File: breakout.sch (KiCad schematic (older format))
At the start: 8 parts, among them CON1 USB-MINI-B, P1 CONN_02X18, P2 CONN_02X18, P3 CONN_02X18, P4 CONN_02X18, P5 CONN_01X17, P6 CONN_01X02, U1 LPC4337JBD144

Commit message: adding components
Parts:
- removed P1, P2, P3, P4: CONN_02X18, Socket_Strips:Socket_Strip_Straight_2x18, symbol CONN_02X18
- removed P5: CONN_01X17, Housings_DFN_QFN:QFN-16-1EP_3x3mm_Pitch0.5mm, symbol CONN_01X17
- added U2: AP3003S-3.3TRE1, SMD_Packages:TO-263-5, symbol AP3003S-3.3TRE1
- added U3: A-DF-09-A/KG-T4S, Custom Footprints:DIN9F, symbol A-DF-09-A/KG-T4S
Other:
- note removed: "Microchip 3.3 V power regulator"
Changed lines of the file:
@@
 LIBS:valves
 LIBS:nxp
+LIBS:diodesinc
+LIBS:assmann
 LIBS:breakout-cache
 EELAYER 25 0
@@
 NoConn ~ 2800 850
 NoConn ~ 2800 950
-$Comp
-L USB-MINI-B CON1
-U 1 1 56013B96
-P 6200 5750
-F 0 "CON1" H 5900 6100 50  0000 C CNN
-F 1 "USB-MINI-B" H 6050 5400 50  0000 C CNN
-F 2 "Connect:USB_Mini-B" H 6200 5650 50  0001 C CNN
-F 3 "" H 6200 5650 50  0000 C CNN
-	1    6200 5750
-	1    0    0    1
-$EndComp
 Wire Wire Line
 	4800 5750 5450 5750
@@
 	5200 7450 4800 7450
 $Comp
-L CONN_02X18 P1
-U 1 1 55FF6B36
-P 1100 1700
-F 0 "P1" H 1100 2650 50  0000 C CNN
-F 1 "CONN_02X18" V 1100 1700 50  0000 C CNN
-F 2 "Socket_Strips:Socket_Strip_Straight_2x18" H 1100 650 60  0001 C CNN
-F 3 "" H 1100 650 60  0000 C CNN
-	1    1100 1700
-	1    0    0    -1
-$EndComp
-$Comp
-L CONN_02X18 P2
-U 1 1 55FF6C44
-P 1100 3650
-F 0 "P2" H 1100 4600 50  0000 C CNN
-F 1 "CONN_02X18" V 1100 3650 50  0000 C CNN
-F 2 "Socket_Strips:Socket_Strip_Straight_2x18" H 1100 2600 60  0001 C CNN
-F 3 "" H 1100 2600 60  0000 C CNN
-	1    1100 3650
-	1    0    0    -1
-$EndComp
-$Comp
-L CONN_02X18 P3
-U 1 1 55FF6CC4
-P 5750 1600
-F 0 "P3" H 5750 2550 50  0000 C CNN
-F 1 "CONN_02X18" V 5750 1600 50  0000 C CNN
-F 2 "Socket_Strips:Socket_Strip_Straight_2x18" H 5750 550 60  0001 C CNN
-F 3 "" H 5750 550 60  0000 C CNN
-	1    5750 1600
-	1    0    0    -1
-$EndComp
-$Comp
-L CONN_02X18 P4
-U 1 1 55FF6D42
-P 5750 3700
-F 0 "P4" H 5750 4650 50  0000 C CNN
-F 1 "CONN_02X18" V 5750 3700 50  0000 C CNN
-F 2 "Socket_Strips:Socket_Strip_Straight_2x18" H 5750 2650 60  0001 C CNN
-F 3 "" H 5750 2650 60  0000 C CNN
-	1    5750 3700
-	1    0    0    -1
-$EndComp
-$Comp
 L CONN_01X02 P6
 U 1 1 55FF7251
@@
 	-1   0    0    1
 $EndComp
-$Comp
-L CONN_01X17 P5
-U 1 1 55FF72F4
-P 7150 2850
-F 0 "P5" H 7150 3750 50  0000 C CNN
-F 1 "CONN_01X17" V 7250 2850 50  0000 C CNN
-F 2 "Housings_DFN_QFN:QFN-16-1EP_3x3mm_Pitch0.5mm" H 7150 2850 60  0001 C CNN
-F 3 "" H 7150 2850 60  0000 C CNN
-	1    7150 2850
-	-1   0    0    1
-$EndComp
 Text Notes 7450 750  0    60   ~ 0
 Power In
-Text Notes 6450 1950 0    60   ~ 0
-Microchip 3.3 V power regulator
+$Comp
+L USB-MINI-B CON1
+U 1 1 56013B96
+P 6200 5750
+F 0 "CON1" H 5900 6100 50  0000 C CNN
+F 1 "USB-MINI-B" H 6050 5400 50  0000 C CNN
+F 2 "Connect:USB_Mini-B" H 6200 5650 50  0001 C CNN
+F 3 "" H 6200 5650 50  0000 C CNN
+	1    6200 5750
+	1    0    0    1
+$EndComp
+$Comp
+L AP3003S-3.3TRE1 U2
+U 1 1 56145B14
+P 6750 2800
+F 0 "U2" H 6750 3750 60  0000 C CNN
+F 1 "AP3003S-3.3TRE1" H 6750 2800 60  0000 C CNN
+F 2 "SMD_Packages:TO-263-5" H 6750 2800 60  0001 C CNN
+F 3 "" H 6750 2800 60  0000 C CNN
+	1    6750 2800
+	1    0    0    -1
+$EndComp
+$Comp
+L A-DF-09-A/KG-T4S U3
+U 1 1 5614B4EE
+P 6400 3450
+F 0 "U3" H 6400 2750 60  0000 C CNN
+F 1 "A-DF-09-A/KG-T4S" H 6400 3450 60  0000 C CNN
+F 2 "Custom Footprints:DIN9F" H 6400 3450 60  0001 C CNN
+F 3 "" H 6400 3450 60  0000 C CNN
+	1    6400 3450
+	1    0    0    -1
+$EndComp
 $EndSCHEMATC

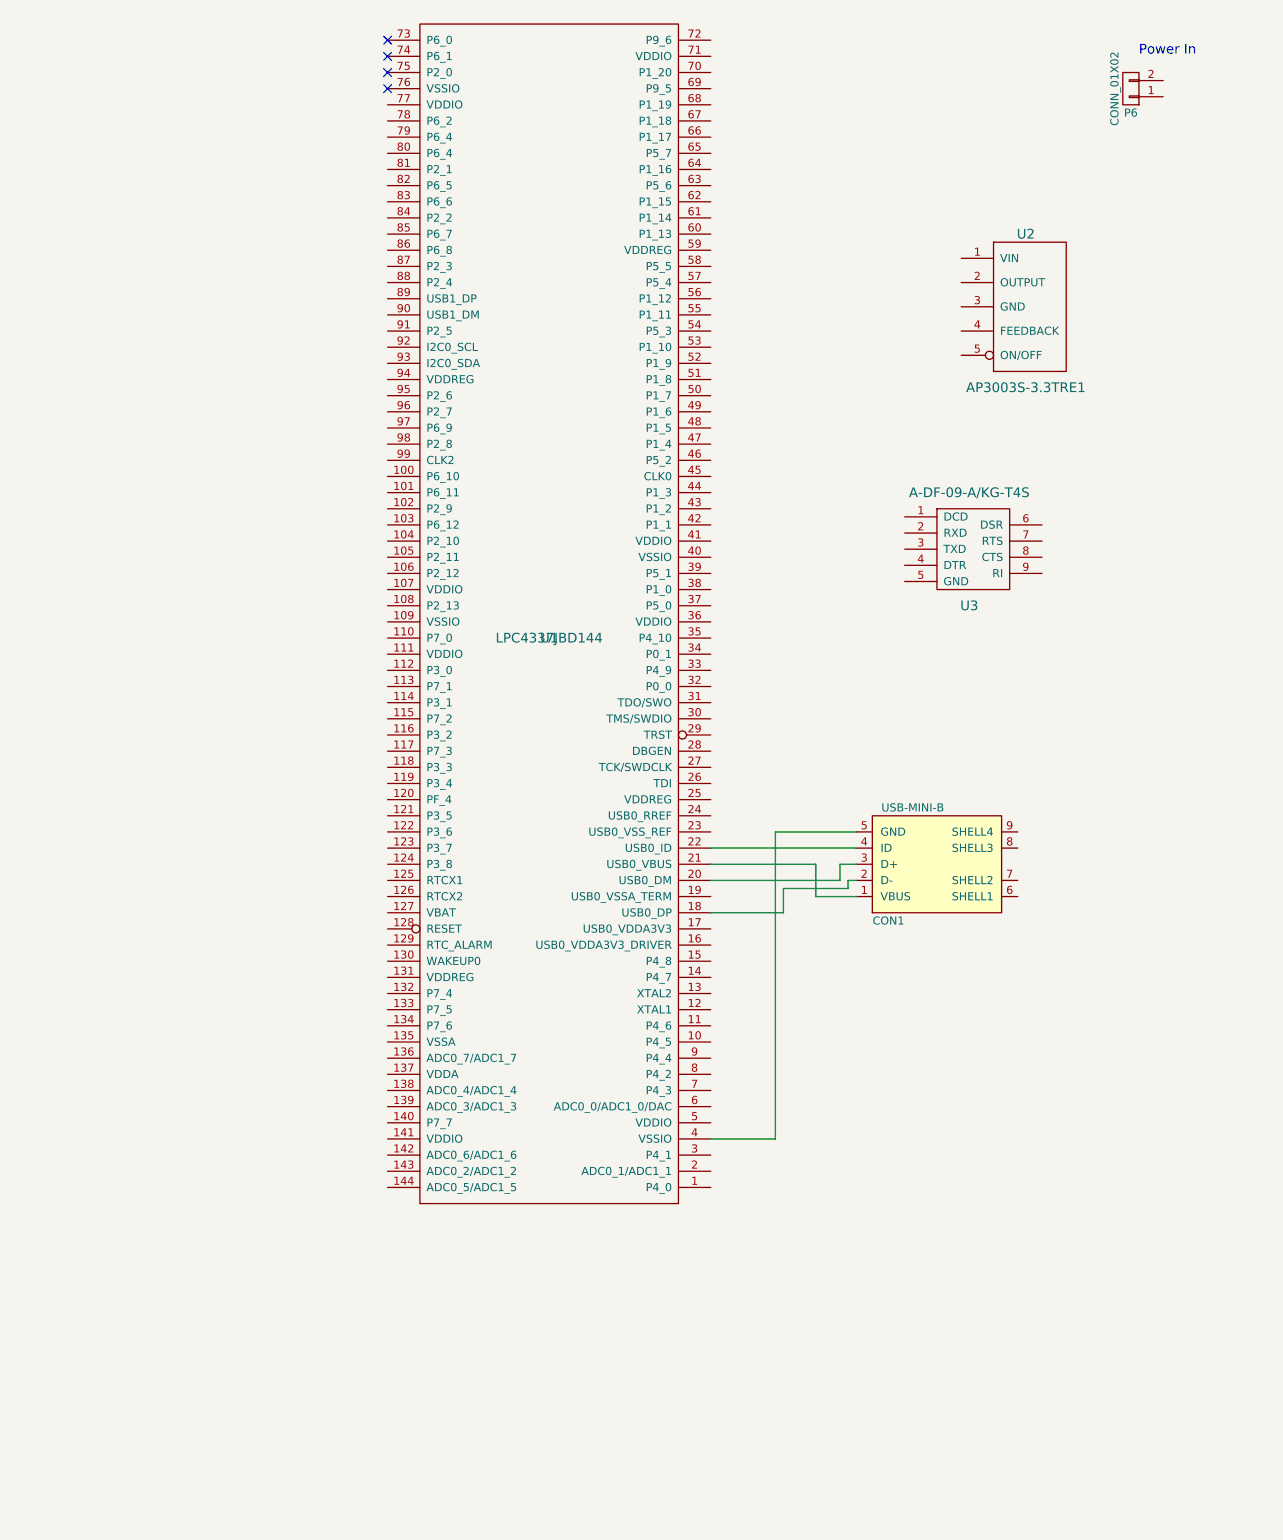
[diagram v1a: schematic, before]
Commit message: working up a netlist of components
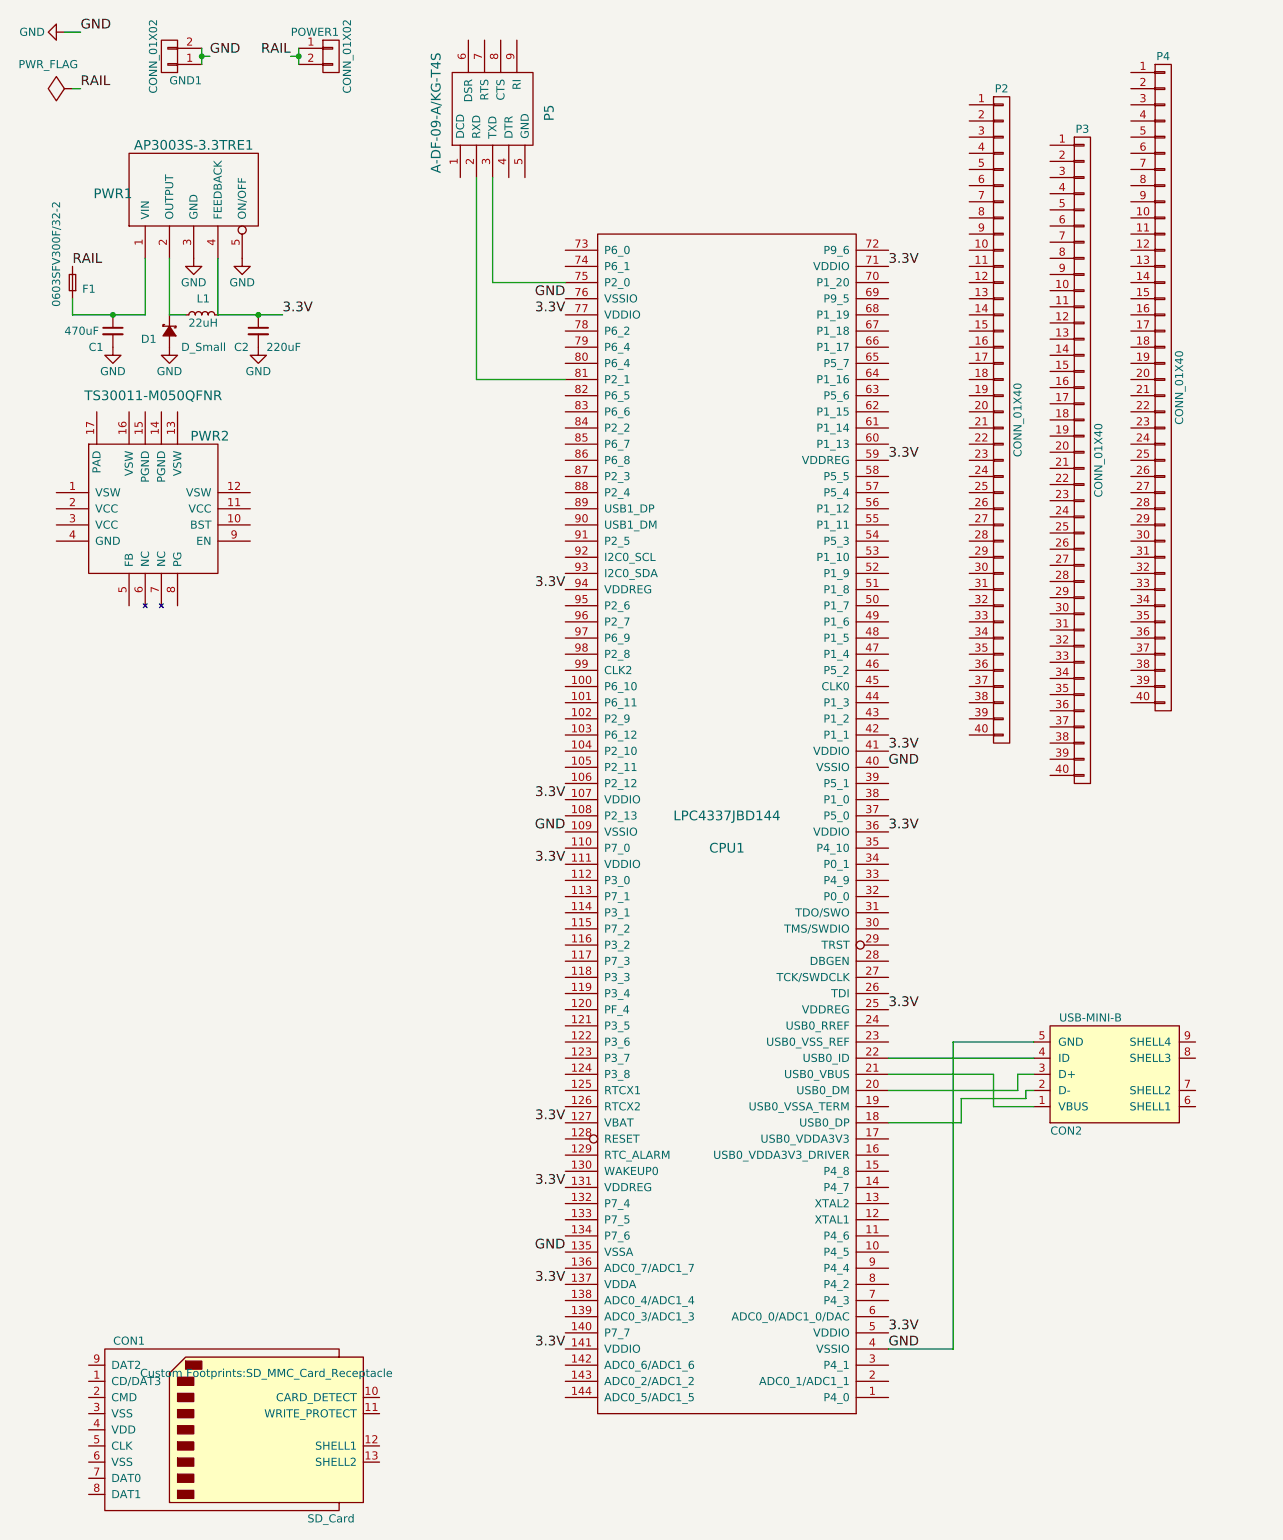
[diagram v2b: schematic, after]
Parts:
- added C1: 470uF, Capacitors_SMD:C_0201, symbol C_Small
- added C2: 220uF, Capacitors_SMD:C_0201, symbol C_Small
- added CON1: SD_Card, Custom Footprints:SD_MMC_Card_Receptacle, symbol SD_Card
- added D1: D_Small, Diodes_ThroughHole:Diode_DO-35_SOD27_Horizontal_RM10, symbol D_Schottky_Small
- added F1: 0603SFV300F/32-2, SMD_Packages:SMD-1206_Pol, symbol F_Small
- added GND1: CONN_01X02, Terminal_Blocks:TerminalBlock_WAGO-236_2Stift_RM5mm_1pol, symbol CONN_01X02
- added L1: 22uH, SMD_Packages:SMD-1206_Pol, symbol L_Small
- added P2, P3, P4: CONN_01X40, Socket_Strips:Socket_Strip_Straight_1x40, symbol CONN_01X40
- added PWR2: TS30011-M050QFNR, Housings_DFN_QFN:QFN-16-1EP_3x3mm_Pitch0.5mm, symbol TS30011-M050QFNR
- renumbered CON1 to CON2, U1 to CPU1, U3 to P5, P6 to POWER1, U2 to PWR1
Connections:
- net 3.3V: now reaches CPU1.107 (VDDIO)
- net 3.3V: now also CPU1.111 (VDDIO), CPU1.127 (VBAT), CPU1.131 (VDDREG), CPU1.137 (VDDA), CPU1.141 (VDDIO), CPU1.25 (VDDREG), CPU1.36 (VDDIO), CPU1.41 (VDDIO), CPU1.5 (VDDIO), CPU1.59 (VDDREG), CPU1.71 (VDDIO), CPU1.77 (VDDIO), CPU1.94 (VDDREG), PWR1.4 (FEEDBACK), C2.1, L1.2
- net GND: now reaches CPU1.109 (VSSIO)
- net GND: now also CON2.5 (GND), CPU1.135 (VSSA), CPU1.4 (VSSIO), CPU1.40 (VSSIO), CPU1.76 (VSSIO), PWR1.3 (GND), PWR1.5 (ON/OFF), C1.2, C2.2, D1.1 (A), GND1.1 (P1), GND1.2 (P2)
- net at CPU1.75 (P2_0): now also P5.3 (TXD)
- net at CPU1.81 (P2_1): now also P5.2 (RXD)
- net RAIL: now reaches POWER1.1 (P1)
- net RAIL: now also POWER1.2 (P2), F1.2
- net at PWR1.1 (VIN): now also C1.1, F1.1
- net at PWR1.2 (OUTPUT): now also D1.2 (C), L1.1
- no-connect marks 4 -> 0
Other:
- note removed: "Power In"
- moved on the sheet: CON2, CPU1, P5, POWER1, PWR1

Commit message: added sd card slot and SPI pins to schematic
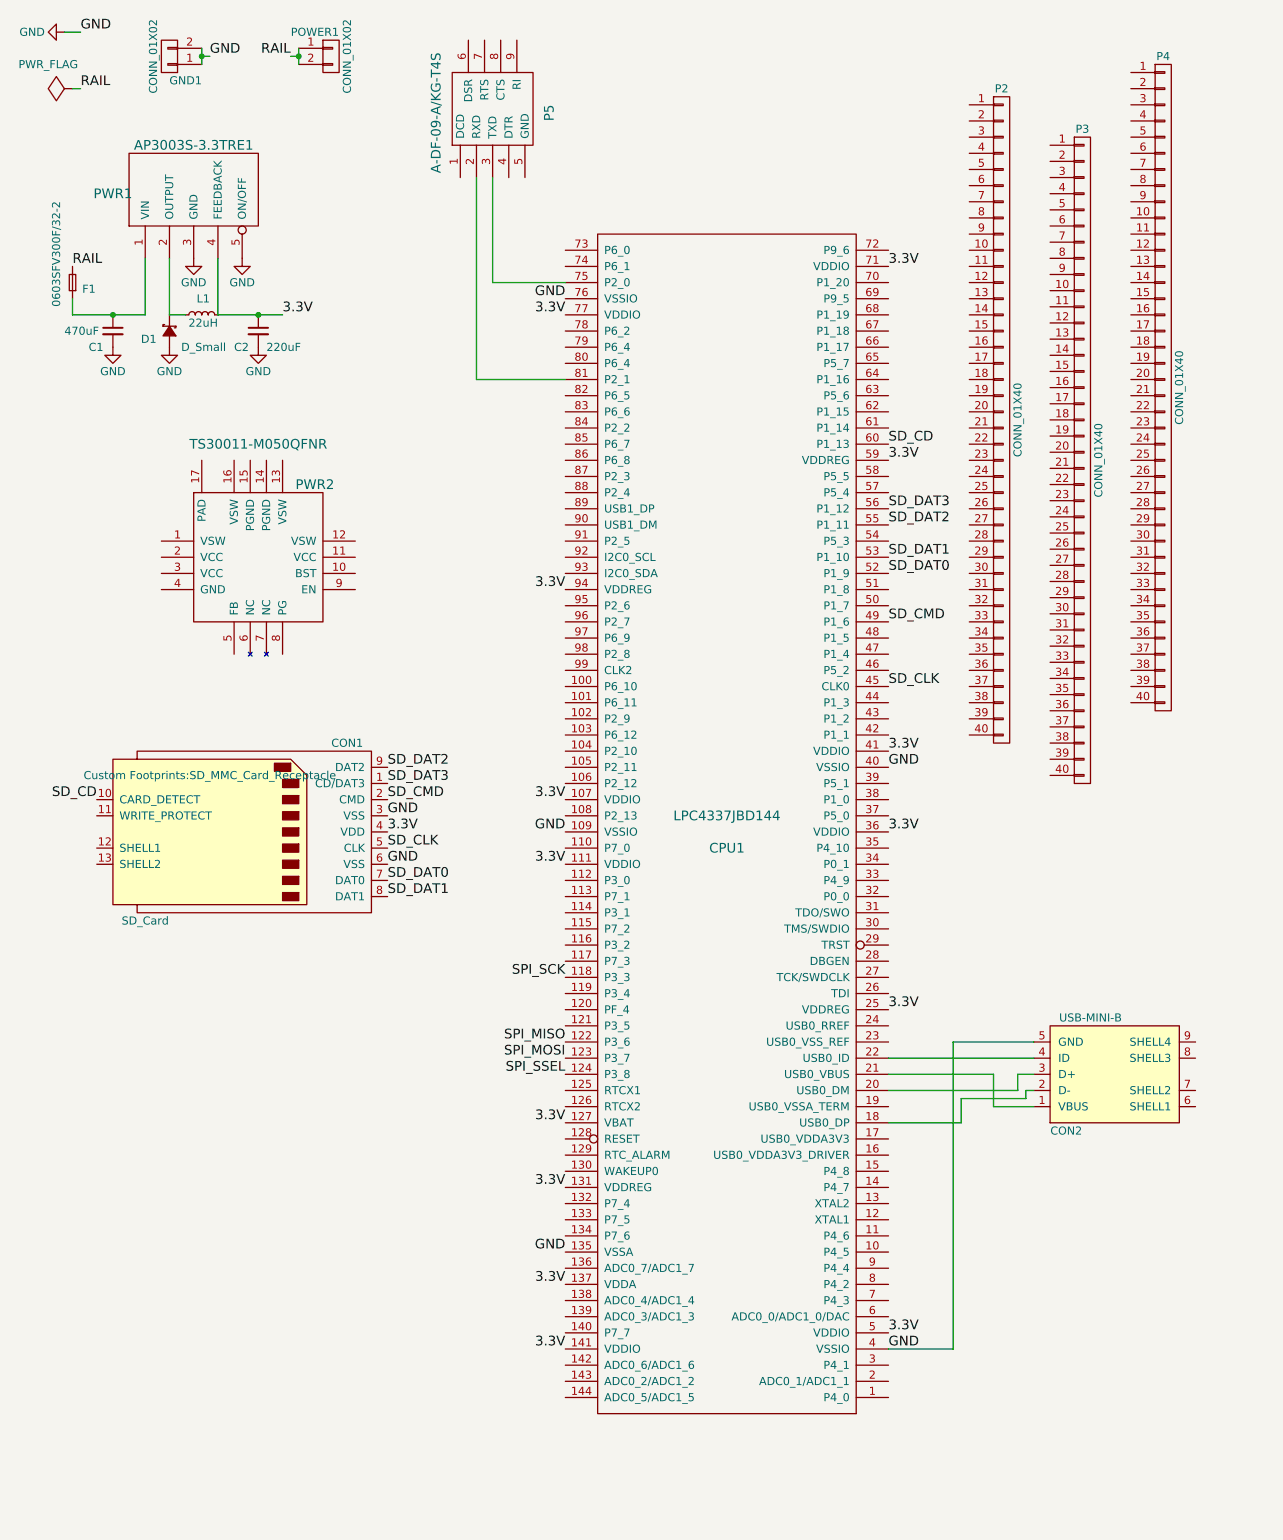
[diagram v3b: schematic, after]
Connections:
- net 3.3V: now also CON1.4 (VDD)
- net GND: now also CON1.3 (VSS), CON1.6 (VSS)
- net SPI_SCK: now reaches CPU1.118 (P3_3)
- net SPI_MISO: now reaches CPU1.122 (P3_6)
- net SPI_MOSI: now reaches CPU1.123 (P3_7)
- net SPI_SSEL: now reaches CPU1.124 (P3_8)
- net SD_CLK: now reaches CPU1.45 (CLK0)
- net SD_CLK: now also CON1.5 (CLK)
- net SD_CMD: now reaches CPU1.49 (P1_6)
- net SD_CMD: now also CON1.2 (CMD)
- net SD_DAT0: now reaches CPU1.52 (P1_9)
- net SD_DAT0: now also CON1.7 (DAT0)
- net SD_DAT1: now reaches CPU1.53 (P1_10)
- net SD_DAT1: now also CON1.8 (DAT1)
- net SD_DAT2: now reaches CPU1.55 (P1_11)
- net SD_DAT2: now also CON1.9 (DAT2)
- net SD_DAT3: now reaches CPU1.56 (P1_12)
- net SD_DAT3: now also CON1.1 (CD/DAT3)
- net SD_CD: now reaches CPU1.60 (P1_13)
- net SD_CD: now also CON1.10 (CARD_DETECT)
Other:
- moved on the sheet: CON1, PWR2
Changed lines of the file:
@@
 L SD_Card CON1
 U 1 1 5614B52D
-P 1850 9250
-F 0 "CON1" H 1200 9800 50  0000 C CNN
-F 1 "SD_Card" H 2450 8700 50  0000 C CNN
-F 2 "Custom Footprints:SD_MMC_Card_Receptacle" H 2050 9600 50  0000 C CNN
-F 3 "" H 1850 9250 60  0000 C CNN
-	1    1850 9250
-	1    0    0    -1
+P 1900 5550
+F 0 "CON1" H 1250 6100 50  0000 C CNN
+F 1 "SD_Card" H 2500 5000 50  0000 C CNN
+F 2 "Custom Footprints:SD_MMC_Card_Receptacle" H 2100 5900 50  0000 C CNN
+F 3 "" H 1900 5550 60  0000 C CNN
+	1    1900 5550
+	-1   0    0    -1
 $EndComp
 $Comp
@@
 L TS30011-M050QFNR PWR2
 U 1 1 561BCBF8
-P 1350 2850
-F 0 "PWR2" H 1700 2600 60  0000 C CNN
-F 1 "TS30011-M050QFNR" H 1350 2850 60  0000 C CNN
-F 2 "Housings_DFN_QFN:QFN-16-1EP_3x3mm_Pitch0.5mm" H 1350 2850 60  0001 C CNN
-F 3 "" H 1350 2850 60  0000 C CNN
-	1    1350 2850
+P 2000 3150
+F 0 "PWR2" H 2350 2900 60  0000 C CNN
+F 1 "TS30011-M050QFNR" H 2000 3150 60  0000 C CNN
+F 2 "Housings_DFN_QFN:QFN-16-1EP_3x3mm_Pitch0.5mm" H 2000 3150 60  0001 C CNN
+F 3 "" H 2000 3150 60  0000 C CNN
+	1    2000 3150
 	1    0    0    -1
 $EndComp
@@
 	1300 2350 1300 2000
 Wire Wire Line
-	850  2350 1300 2350
+	850  2350 1100 2350
+Wire Wire Line
+	1100 2350 1300 2350
 Wire Wire Line
 	850  2350 850  2250
 Wire Wire Line
-	1750 2350 2150 2350
+	1750 2350 2000 2350
+Wire Wire Line
+	2000 2350 2150 2350
 $Comp
 L C_Small C2
@@
 	850  950  900  950
 Wire Wire Line
-	1650 700  1650 800
+	1650 700  1650 750
+Wire Wire Line
+	1650 750  1650 800
 Wire Wire Line
 	1650 750  1700 750
@@
 GND
 Wire Wire Line
-	2250 700  2250 800
+	2250 700  2250 750
+Wire Wire Line
+	2250 750  2250 800
 Wire Wire Line
 	2250 750  2200 750
@@
 Wire Wire Line
 	3350 2750 3900 2750
+Text Label 3900 6450 2    60   ~ 0
+SPI_SCK
+Text Label 3900 6850 2    60   ~ 0
+SPI_MISO
+Text Label 3900 6950 2    60   ~ 0
+SPI_MOSI
+Text Label 3900 7050 2    60   ~ 0
+SPI_SSEL
+Text Label 2800 5150 0    60   ~ 0
+SD_DAT2
+Text Label 2800 5250 0    60   ~ 0
+SD_DAT3
+Text Label 2800 5850 0    60   ~ 0
+SD_DAT0
+Text Label 2800 5950 0    60   ~ 0
+SD_DAT1
+Text Label 1000 5350 2    60   ~ 0
+SD_CD
+Text Label 2800 5350 0    60   ~ 0
+SD_CMD
+Text Label 2800 5650 0    60   ~ 0
+SD_CLK
+Text Label 2800 5550 0    60   ~ 0
+3.3V
+Text Label 2800 5750 0    60   ~ 0
+GND
+Text Label 2800 5450 0    60   ~ 0
+GND
+Text Label 5900 4650 0    60   ~ 0
+SD_CLK
+Text Label 5900 3850 0    60   ~ 0
+SD_DAT1
+Text Label 5900 3950 0    60   ~ 0
+SD_DAT0
+Text Label 5900 4250 0    60   ~ 0
+SD_CMD
+Text Label 5900 3550 0    60   ~ 0
+SD_DAT3
+Text Label 5900 3650 0    60   ~ 0
+SD_DAT2
+Text Label 5900 3150 0    60   ~ 0
+SD_CD
 $EndSCHEMATC
